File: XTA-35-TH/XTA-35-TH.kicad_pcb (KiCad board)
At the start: 4 copper layers, 100 x 98.7 mm, 36 parts, among them J1 XTA_Connector, J2 XTA Power, J3 LED, J4 SD0, J5 SD1, J6 Debug, SW1 Config, SW2 Boot Internal, SW3 Reset, U1 74LVC245, U2 74LVC245, U3 74HCT125, U4 74HC165, U5 Raspberry Pi Pico

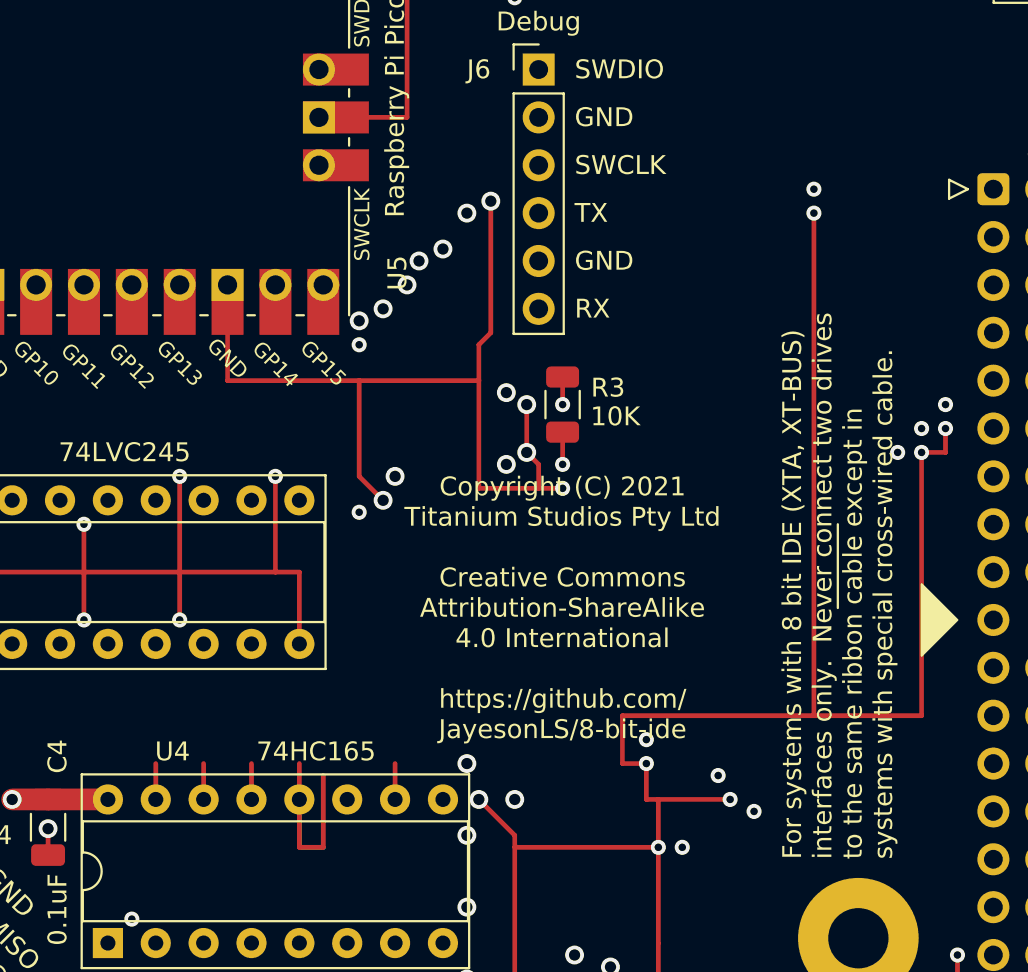
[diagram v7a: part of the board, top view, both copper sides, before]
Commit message: Minor silkscreen changes.
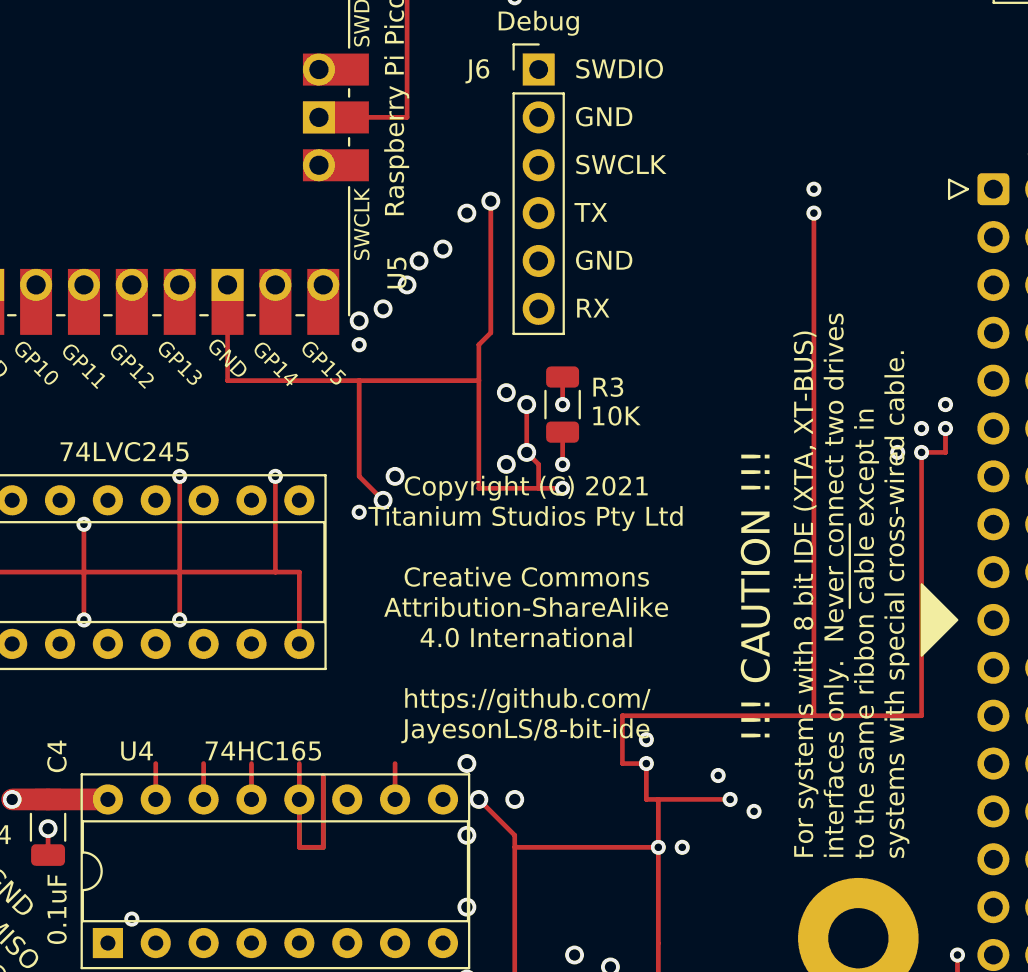
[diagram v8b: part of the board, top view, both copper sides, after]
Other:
- board text added: "!!! CAUTION !!!"
